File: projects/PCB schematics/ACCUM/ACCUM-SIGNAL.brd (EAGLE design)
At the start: 43.2 x 64.4 mm, 31 parts, among them IC1 OPA454, J1 2P_1-770166-0, J2 2P_1-770166-0, J3 2P_1-770166-0, J4 2P_1-770166-0, Q1 IRLZ44Z, X1 5566-2

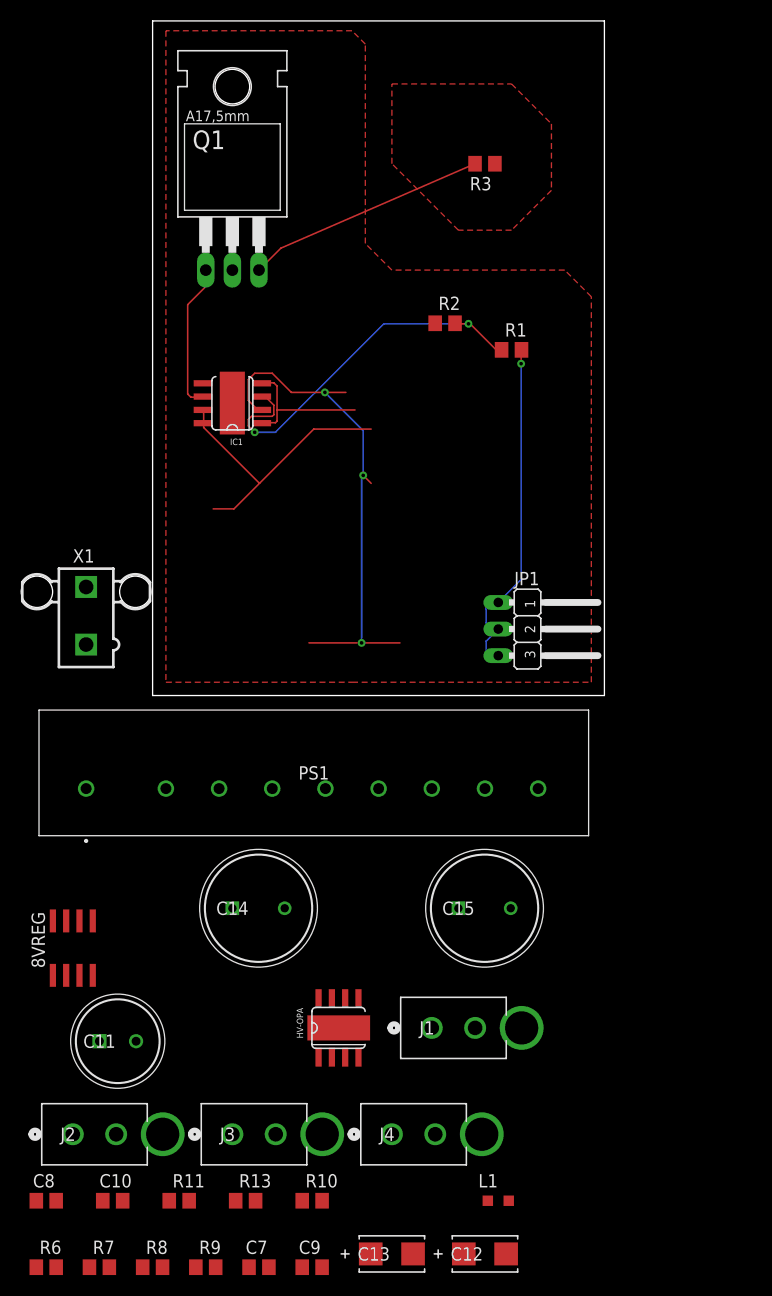
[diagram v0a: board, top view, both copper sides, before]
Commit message: ACCUM - Added POWER board.
ACCUM - POWER and SIGNAL complete.

Two separate boards have been created. One for Powerex, and one for signal sampling.
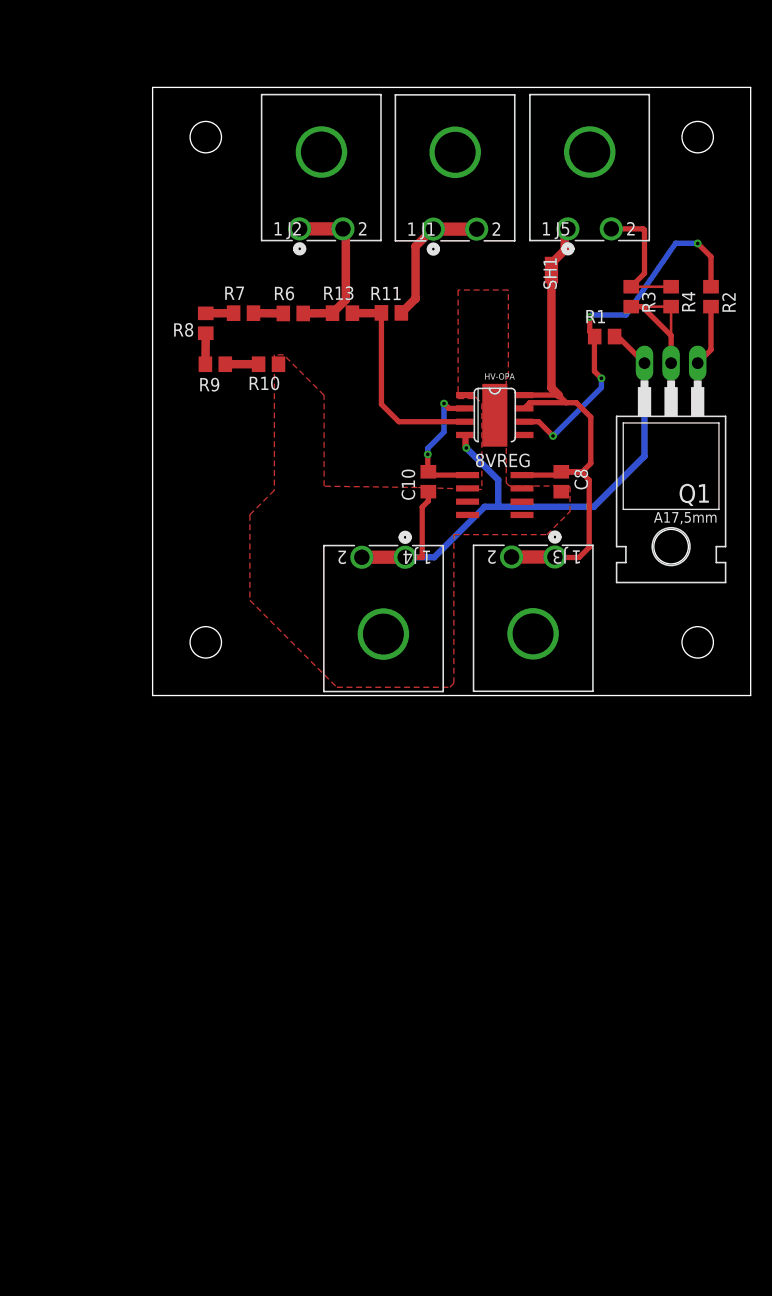
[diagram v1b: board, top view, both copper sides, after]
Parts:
- removed C11: EEU-FS1H221L, EEU-FS1H221L:CAPPRD350W65D800H2200
- removed C12, C13: T491C106K020AT, T491C106K020AT:CAPT6032N
- removed C14, C15: EKXF451ELL100MJ20S, EKXF451ELL100MJ20S:CAPPRD500W60D1025H2150
- removed C7, C9: 1uF, rcl:C0805
- removed IC1: OPA454, OPA454:SO08GP
- removed JP1: (no value), jumper:JP2W
- removed L1: 1mH, rcl:L2012C
- removed PS1: M57184N-715B, M57184N-715B:M57184N715B
- removed X1: 5566-2, con-molex:5566-2
- added J5: 2P(90DEG)_1-770966-0, con-MATE-N-LOK:CON2_1X2_P163_RAMNL
- added R4: 5.6k, rcl:R0805
- added SH1: SHORTT5, shorts:SHORT_TOP-50
- 8VREG: value L78L08ACD -> L78L08ABD13TR
- C8: value 0.1uF -> 0.33uF
- J1, J2, J3, J4: value 2P_1-770166-0 -> 2P(90DEG)_1-770966-0; device con-MATE-N-LOK:CON2_1X2_P163_VMNL-1MTG -> con-MATE-N-LOK:CON2_1X2_P163_RAMNL
- R1: value 680k -> 100k
- R2: value 100k -> 100
- R3: value (none) -> 470
- moved R6 94.1 mm to (13.4, 36.5), turned to 180 degrees
- moved R7 92.2 mm to (8.69, 36.5), turned to 180 degrees
- moved R8 90.3 mm to (5.08, 35.6), turned to 270 degrees
- moved J2 90.3 mm to (18.2, 44.6)
- moved R11 87.2 mm to (22.8, 36.6)
- moved R9 86.3 mm to (5.99, 31.6)
- moved R13 85.3 mm to (18.1, 36.5)
- moved C8 84.5 mm to (39.0, 20.4), turned to 270 degrees
- moved R10 80.0 mm to (11.1, 31.6)
- moved J1 76.4 mm to (31.0, 44.6)
- moved C10 75.0 mm to (26.3, 20.4), turned to 270 degrees
- moved J3 61.3 mm to (34.3, 13.2), turned to 180 degrees
- moved HV-OPA 60.4 mm to (32.7, 26.8), turned to 270 degrees
- moved 8VREG 59.1 mm to (32.7, 19.2), turned to 270 degrees
- moved J4 55.2 mm to (20.0, 13.2), turned to 180 degrees
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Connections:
- removed net +60V-POST-AIR_INDICATOR: IC1.6, Q1.G
- removed net ACCUM_LIGHT: Q1.D, X1.1, X1.2
- removed net GND: R2.1, R3.1
- removed net HV+: C14.1, J1.1, J1.2, PS1.1
- removed net HV_POST_AIR: JP1.1, JP1.2, JP1.3, R1.2
- removed net N$2: L1.1, PS1.6
- removed net N$6: Q1.S, R3.2
- removed net THERMAL: HV-OPA.THERMAL
- removed net V+: IC1.7, IC1.8
- removed net VDIV_SIGNAL: IC1.3, R1.1, R2.2
- new net LED+: J5.1, SH1.2
- new net LED-: J5.2, R3.1, R4.1
- net +15V-NONISO: now also J3.1, J3.2, SH1.1; no longer C11.1, C13.1, C7.1, PS1.10
- net +8V: no longer C12.1, C9.1, IC1.2
- net HV+_POST_AIR+: now also J1.1, J1.2; no longer J2.1, J2.2
- net HV-: now also HV-OPA.THERMAL, Q1.S, R1.1; no longer C11.2, C12.2, C13.2, C15.2, C7.2, C9.2, IC1.1, IC1.4, PS1.4
- net HV-_POST_AIR-: now also J2.1, J2.2; no longer J3.1, J3.2
- net N$1: now also Q1.D, R3.2, R4.2; no longer L1.2, PS1.8
- net N$3: now also Q1.G, R2.1; no longer C14.2, C15.1
- net N$9: now also R1.2, R2.2
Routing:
- net +15V-NONISO: track 0.00 -> 51.8 mm
- net HV-: track 13.9 -> 60.1 mm, vias 0 -> 1
- net VDIV_SIGNAL: track 36.7 -> 0.00 mm, vias 2 -> 0
- net +8V: track 49.3 -> 13.3 mm, vias 3 -> 2
- net N$9: track 0.00 -> 35.8 mm, vias 0 -> 4
- net HV_POST_AIR: track 33.8 -> 0.00 mm, vias 1 -> 0
- net V+: track 27.6 -> 0.00 mm
- net N$6: track 23.2 -> 0.00 mm
- net SIGNAL_VDIV: track 0.00 -> 20.2 mm
- net HV-_POST_AIR-: track 0.00 -> 15.6 mm
- net N$1: track 0.00 -> 15.5 mm
- net +60V-POST-AIR_INDICATOR: track 14.2 -> 0.00 mm
- net HV+_POST_AIR+: track 0.00 -> 13.4 mm
- net LED-: track 0.00 -> 13.0 mm
- net N$3: track 0.00 -> 5.93 mm
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- added copper zone on layer 1, net HV-
- removed copper zone on layer 1, net GND
- removed copper zone on layer 1, net VCC
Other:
- board size 43.2 x 64.4 mm -> 57.1 x 58.1 mm

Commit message: ACCUM - Rev A.
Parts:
- moved R10 2.54 mm to (11.1, 34.2)
- moved R9 2.54 mm to (5.99, 34.2)
- moved R11 2.54 mm to (22.8, 39.1)
- moved R13 2.54 mm to (18.1, 39.1)
- moved R6 2.54 mm to (13.4, 39.0)
- moved R7 2.54 mm to (8.69, 39.1)
- moved R8 2.54 mm to (5.08, 38.1)
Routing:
- net HV-_POST_AIR-: track 15.6 -> 13.1 mm
- net HV+_POST_AIR+: track 13.4 -> 10.9 mm
- net SIGNAL_VDIV: track 20.2 -> 21.3 mm
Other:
- board text added: "1. HV- 2. +15V-NONISO"
- board text added: "1. HV-_POST_AIR- 2. HV+_POST_AIR+ 3. LED+, LED-"
- board text added: "Accumulator Indicator Light Rev A: April 11th, 2019"
- board text added: "Author: github.com/michaelpass"

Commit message: ACCUM - BOM Created (Signal)
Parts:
- Q1: value IRLZ44Z -> IRFZ44Z
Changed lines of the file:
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@@
 <attribute name="SPICEPREFIX" value="R" x="53.34" y="38.1" size="1.778" layer="27" rot="R90" display="off"/>
 </element>
-<element name="Q1" library="transistor-power" library_urn="urn:adsk.eagle:library:400" package="TO220BH" package3d_urn="urn:adsk.eagle:package:29490/1" value="IRLZ44Z" x="49.53" y="25.4" smashed="yes" rot="R180">
+<element name="Q1" library="transistor-power" library_urn="urn:adsk.eagle:library:400" package="TO220BH" package3d_urn="urn:adsk.eagle:package:29490/1" value="IRFZ44Z" x="49.53" y="25.4" smashed="yes" rot="R180">
 <attribute name="NAME" x="53.34" y="20.193" size="1.778" layer="25" ratio="10" rot="R180"/>
 <attribute name="VALUE" x="53.467" y="22.86" size="1.778" layer="27" ratio="10" rot="R180"/>

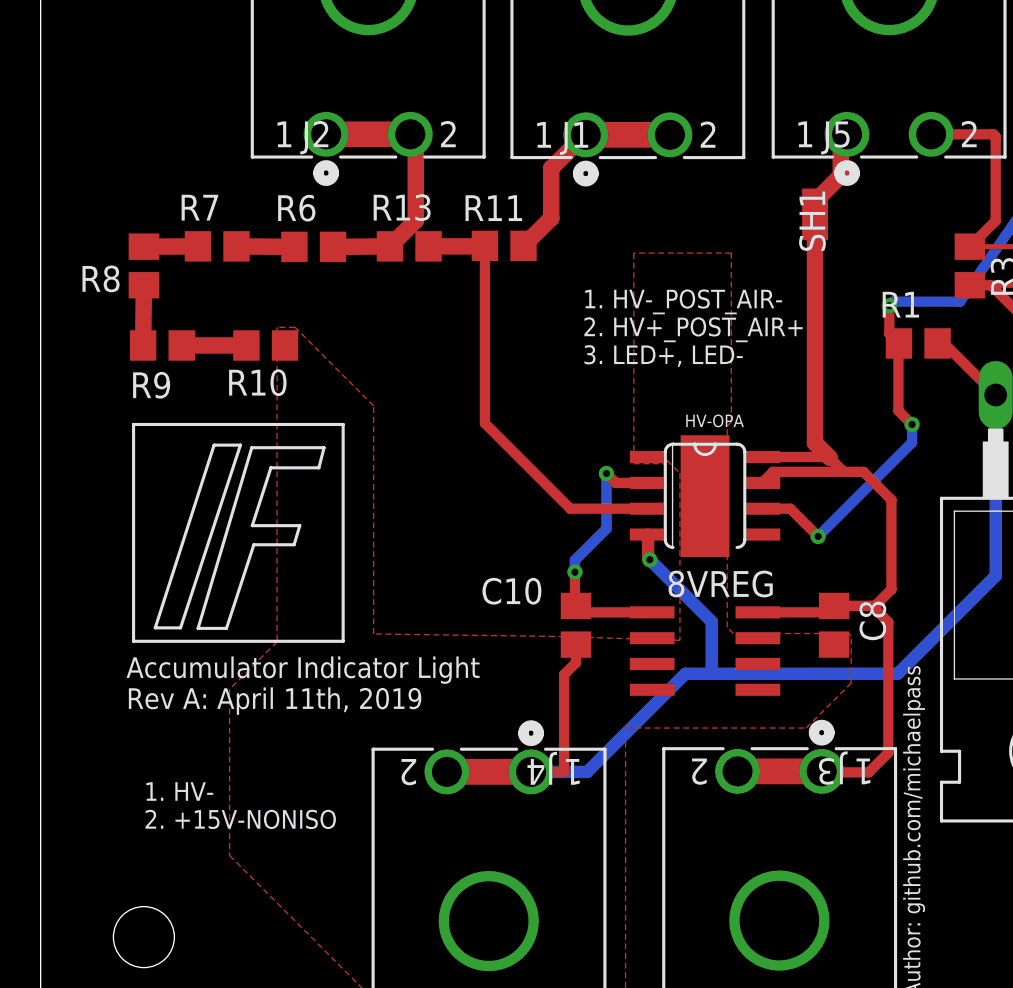
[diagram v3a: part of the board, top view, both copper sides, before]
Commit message: TSAL - Added in fuses.
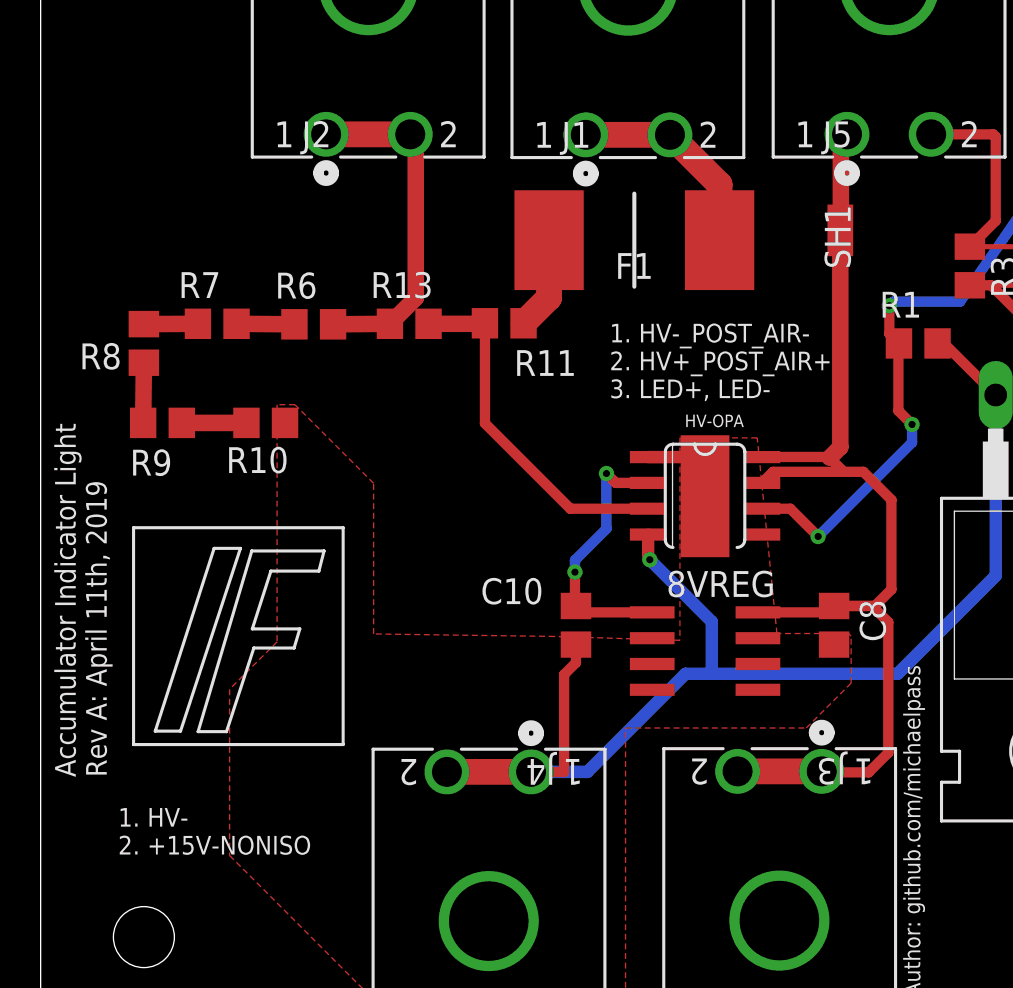
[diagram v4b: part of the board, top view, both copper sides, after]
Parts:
- added F1: 0885001.DR, 0885001.DR:FUSC10948X488N
- moved R10 3.81 mm to (11.1, 30.4)
- moved R11 3.81 mm to (22.8, 35.3)
- moved R6 3.81 mm to (13.4, 35.2)
- moved R8 3.81 mm to (5.08, 34.3)
- moved R9 3.81 mm to (5.99, 30.4)
- moved R13 3.81 mm to (18.1, 35.3)
- moved R7 3.81 mm to (8.69, 35.3)
- moved SH1 1.47 mm to (39.3, 39.9)
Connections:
- new net N$2: F1.2, R11.2
- net HV+_POST_AIR+: now also F1.1; no longer R11.2
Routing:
- net HV-: track 60.1 -> 65.3 mm
- net N$2: track 0.00 -> 4.61 mm
- net SIGNAL_VDIV: track 21.3 -> 17.5 mm
- net HV-_POST_AIR-: track 13.1 -> 16.9 mm
- net +15V-NONISO: track 51.8 -> 51.0 mm
- net HV+_POST_AIR+: track 10.9 -> 10.4 mm
